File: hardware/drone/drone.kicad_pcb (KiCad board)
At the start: 2 copper layers, 2 parts, among them U1 STM32N645I0, U2 SX1262IMLTRT

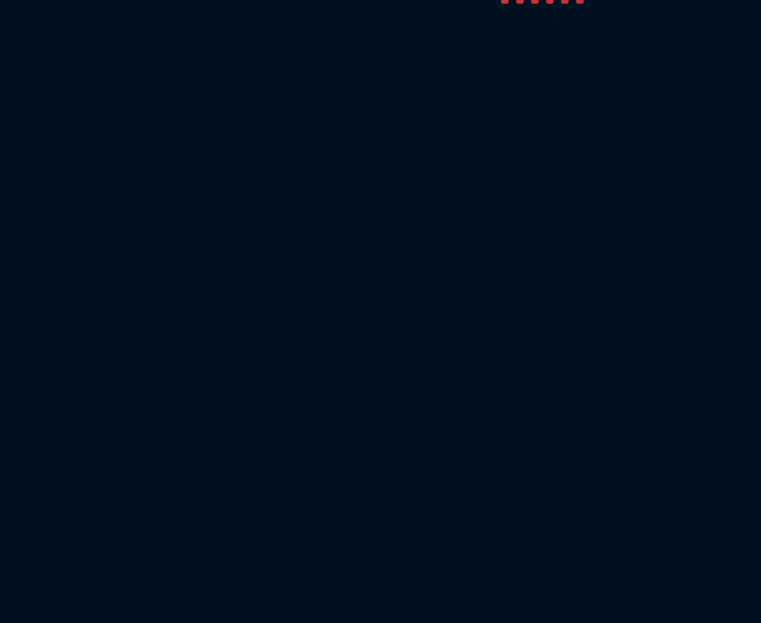
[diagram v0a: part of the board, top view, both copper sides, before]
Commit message: Continued PDN and started camera schematic
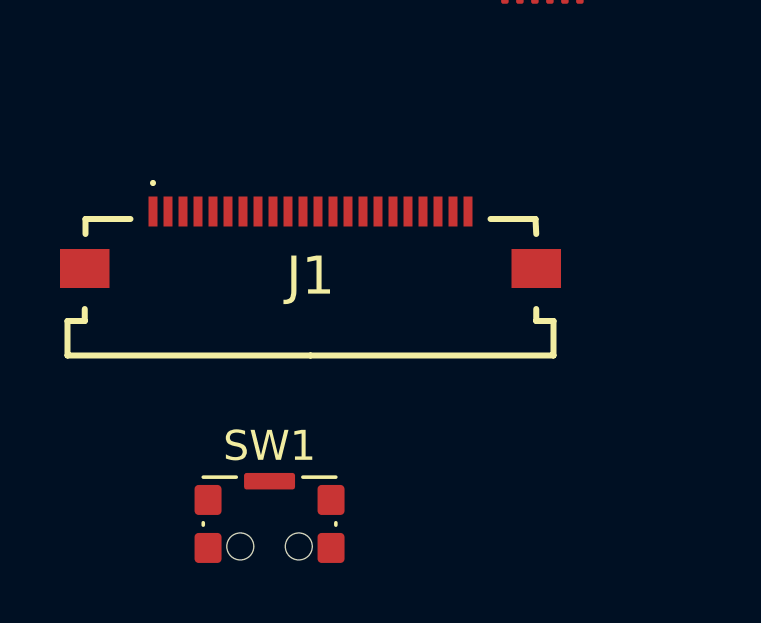
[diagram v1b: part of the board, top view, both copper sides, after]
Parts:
- added J1: 54548-2272, 54548-2272:545482272, F.Cu at (122.3, 106.8)
- added SW1: SW_MEC_5E, Button_Switch_SMD:SW_SPST_CK_KMS2xxGP, F.Cu at (120.9, 114.8)
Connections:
- U1 pad A1: (no net) -> unconnected-(U1MISC-PDR_ON-PadA1)
- U1 pad A14: unconnected-(U1Ground-VSS-PadA14) -> GND
- U1 pad A2: (no net) -> unconnected-(U1USB-OTG2_HSDM-PadA2)
- U1 pad A3: (no net) -> unconnected-(U1MISC-NC-PadA3)
- U1 pad A5: (no net) -> unconnected-(U1USB-OTG1_HSDM-PadA5)
- U1 pad A6: (no net) -> unconnected-(U1USB-UCPD1_CC1-PadA6)
- U1 pad B2: (no net) -> unconnected-(U1USB-OTG2_HSDP-PadB2)
- U1 pad B3: (no net) -> unconnected-(U1USB-OTG1_ID-PadB3)
- U1 pad B4: (no net) -> unconnected-(U1USB-OTG2_TXRTUNE-PadB4)
- U1 pad B5: (no net) -> unconnected-(U1USB-OTG1_HSDP-PadB5)
- U1 pad B6: (no net) -> unconnected-(U1USB-UCPD1_CC2-PadB6)
- U1 pad C4: (no net) -> unconnected-(U1MISC-NC-PadC4)
- U1 pad C5: (no net) -> unconnected-(U1USB-OTG2_ID-PadC5)
- U1 pad D2: unconnected-(U1Power-VFBSMPS-PadD2) -> VDDCORE
- U1 pad D3: (no net) -> unconnected-(U1MISC-BOOT0-PadD3)
- U1 pad D5: (no net) -> unconnected-(U1USB-OTG1_TXRTUNE-PadD5)
- U1 pad E3: (no net) -> unconnected-(U1MISC-PWR_ON-PadE3)
- U1 pad E4: (no net) -> /MCU/RESET
- U1 pad E7: unconnected-(U1Ground-VSS-PadE7) -> GND
- U1 pad F1: unconnected-(U1Ground-VSSSMPS-PadF1) -> GND
- U1 pad F10: unconnected-(U1Ground-VSS-PadF10) -> GND
- U1 pad F2: unconnected-(U1Ground-VSSSMPS-PadF2) -> GND
- U1 pad F3: unconnected-(U1Ground-VSSSMPS-PadF3) -> GND
- U1 pad F4: unconnected-(U1Ground-VSSSMPS-PadF4) -> GND
- U1 pad F5: unconnected-(U1Ground-VSSAON-PadF5) -> GND
- U1 pad G1: unconnected-(U1Power-VLXSMPS-PadG1) -> Net-(C6-Pad2)
- U1 pad G10: unconnected-(U1Power-VDD-PadG10) -> VDDIO
- U1 pad G11: unconnected-(U1Power-VDD-PadG11) -> VDDIO
- U1 pad G12: unconnected-(U1Power-VDD-PadG12) -> VDDIO
- U1 pad G2: unconnected-(U1Power-VLXSMPS-PadG2) -> Net-(C6-Pad2)
- U1 pad G3: unconnected-(U1Power-VLXSMPS-PadG3) -> Net-(C6-Pad2)
- U1 pad G4: unconnected-(U1Power-VLXSMPS-PadG4) -> Net-(C6-Pad2)
- U1 pad H1: unconnected-(U1Power-VDDSMPS-PadH1) -> VDD1V8_SMPS
- U1 pad H10: unconnected-(U1Ground-VSS-PadH10) -> GND
- U1 pad H11: unconnected-(U1Ground-VSS-PadH11) -> GND
- U1 pad H2: unconnected-(U1Power-VDDSMPS-PadH2) -> VDD1V8_SMPS
- U1 pad H3: unconnected-(U1Power-VDDSMPS-PadH3) -> VDD1V8_SMPS
- U1 pad H4: unconnected-(U1Power-VDDSMPS-PadH4) -> VDD1V8_SMPS
- U1 pad K10: unconnected-(U1Ground-VSS-PadK10) -> GND
- U1 pad K5: unconnected-(U1Ground-VSS-PadK5) -> GND
- U1 pad K6: unconnected-(U1Power-VDDCORE-PadK6) -> VDDCORE
- U1 pad K7: unconnected-(U1Power-VDDCORE-PadK7) -> VDDCORE
- U1 pad K8: unconnected-(U1Power-VDDCORE-PadK8) -> VDDCORE
- U1 pad K9: unconnected-(U1Power-VDDCORE-PadK9) -> VDDCORE
- U1 pad L7: unconnected-(U1Power-VDDCORE-PadL7) -> VDDCORE
- U1 pad M4: unconnected-(U1Ground-VSSA-PadM4) -> GND
- U1 pad N2: unconnected-(U1CSI-CSI_D1N-PadN2) -> /Camera/CSI_D1N
- U1 pad N3: unconnected-(U1CSI-CSI_CKN-PadN3) -> /Camera/CSI_CKN
- U1 pad N4: unconnected-(U1CSI-CSI_D0N-PadN4) -> /Camera/CSI_D0N
- U1 pad N6: unconnected-(U1Power-VDDCSI-PadN6) -> VDDCORE
- U1 pad P1: unconnected-(U1Ground-VSS-PadP1) -> GND
- U1 pad P14: unconnected-(U1Ground-VSS-PadP14) -> GND
- U1 pad P2: unconnected-(U1CSI-CSI_D1P-PadP2) -> /Camera/CSI_D1P
- U1 pad P3: unconnected-(U1CSI-CSI_CKP-PadP3) -> /Camera/CSI_CKP
- U1 pad P4: unconnected-(U1CSI-CSI_D0P-PadP4) -> /Camera/CSI_D0P

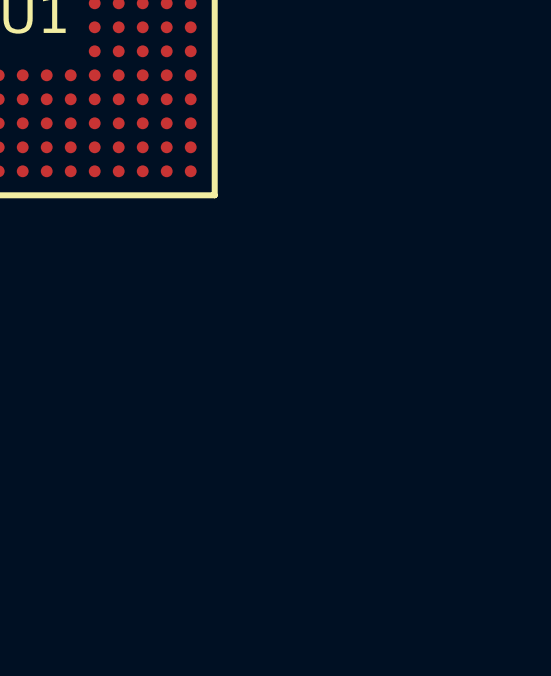
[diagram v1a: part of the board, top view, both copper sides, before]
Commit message: Created symbol for CC3350. Almost finished schematic for OSPI
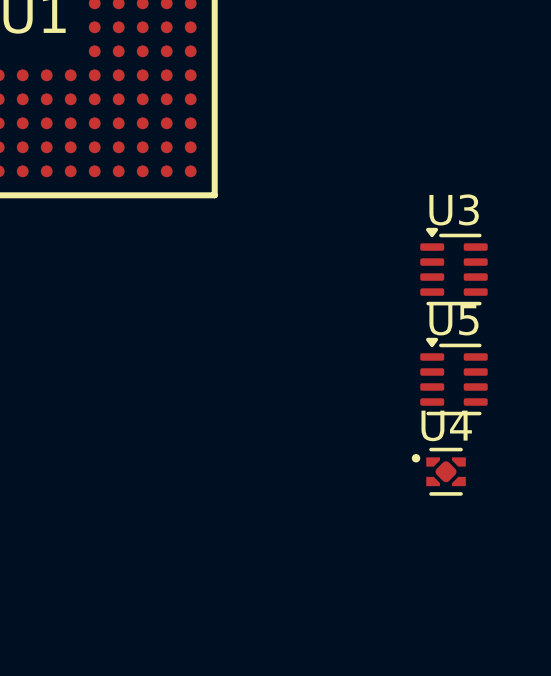
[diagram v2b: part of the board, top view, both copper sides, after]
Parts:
- added U3: TPS628303, Package_SON:Texas_VSON-HR-8_1.5x2mm_P0.5mm, F.Cu at (158.0, 104.0)
- added U4: TPS7A2118PQWDSGRQ1, Package_SON:Texas_X2SON-4_1x1mm_P0.65mm, F.Cu at (157.7, 110.7)
- added U5: TPS628303, Package_SON:Texas_VSON-HR-8_1.5x2mm_P0.5mm, F.Cu at (158.0, 107.7)
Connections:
- U1 pad A4: unconnected-(U1Power-VDD33USB-PadA4) -> GND
- U1 pad C2: unconnected-(U1Power-VBAT-PadC2) -> VDDA1V8
- U1 pad D1: unconnected-(U1Power-V08CAP-PadD1) -> Net-(U1Power-V08CAP)
- U1 pad D4: unconnected-(U1Power-VDDA18USB-PadD4) -> GND
- U1 pad E1: unconnected-(U1Power-VDDA18PMU-PadE1) -> VDDA1V8PMU
- U1 pad E5: unconnected-(U1Power-VDDA18AON-PadE5) -> VDDA1V8
- U1 pad E8: unconnected-(U1Power-VDDIO4-PadE8) -> VDD1V8
- U1 pad E9: unconnected-(U1Power-VDDIO4-PadE9) -> VDD1V8
- U1 pad G10: VDDIO -> VDDA1V8
- U1 pad G11: VDDIO -> VDDA1V8
- U1 pad G12: VDDIO -> VDDA1V8
- U1 pad H1: VDD1V8_SMPS -> VDD1V8
- U1 pad H2: VDD1V8_SMPS -> VDD1V8
- U1 pad H3: VDD1V8_SMPS -> VDD1V8
- U1 pad H4: VDD1V8_SMPS -> VDD1V8
- U1 pad J10: unconnected-(U1Power-VDDIO3-PadJ10) -> VDD1V8
- U1 pad J11: unconnected-(U1Power-VDDIO3-PadJ11) -> VDD1V8
- U1 pad M1: unconnected-(U1Power-VREF+-PadM1) -> VDD1V8
- U1 pad M3: unconnected-(U1Power-VDDA18ADC-PadM3) -> VDD1V8
- U1 pad N1: unconnected-(U1Power-VREF--PadN1) -> GND
- U1 pad P5: unconnected-(U1Power-VDDA18CSI-PadP5) -> VDD1V8

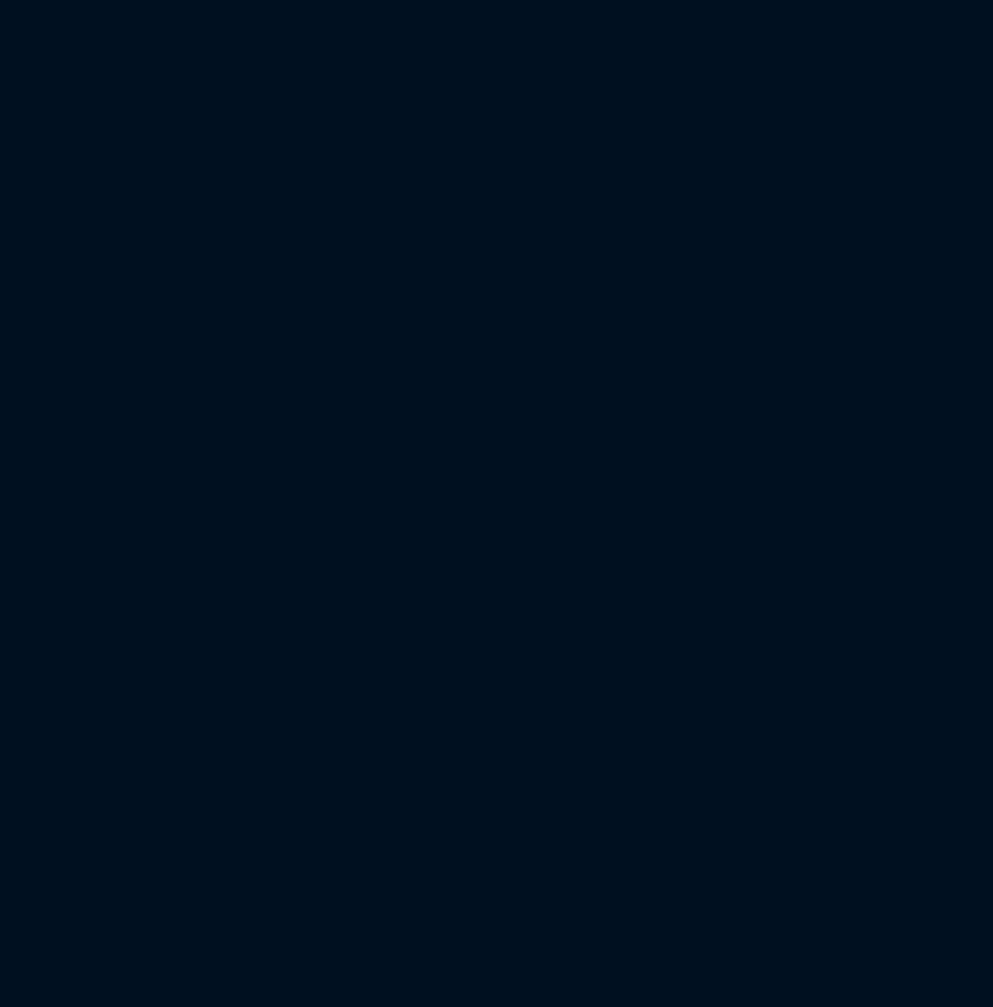
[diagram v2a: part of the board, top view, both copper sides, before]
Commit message: Fixed SMPS and LDO sequencing issues
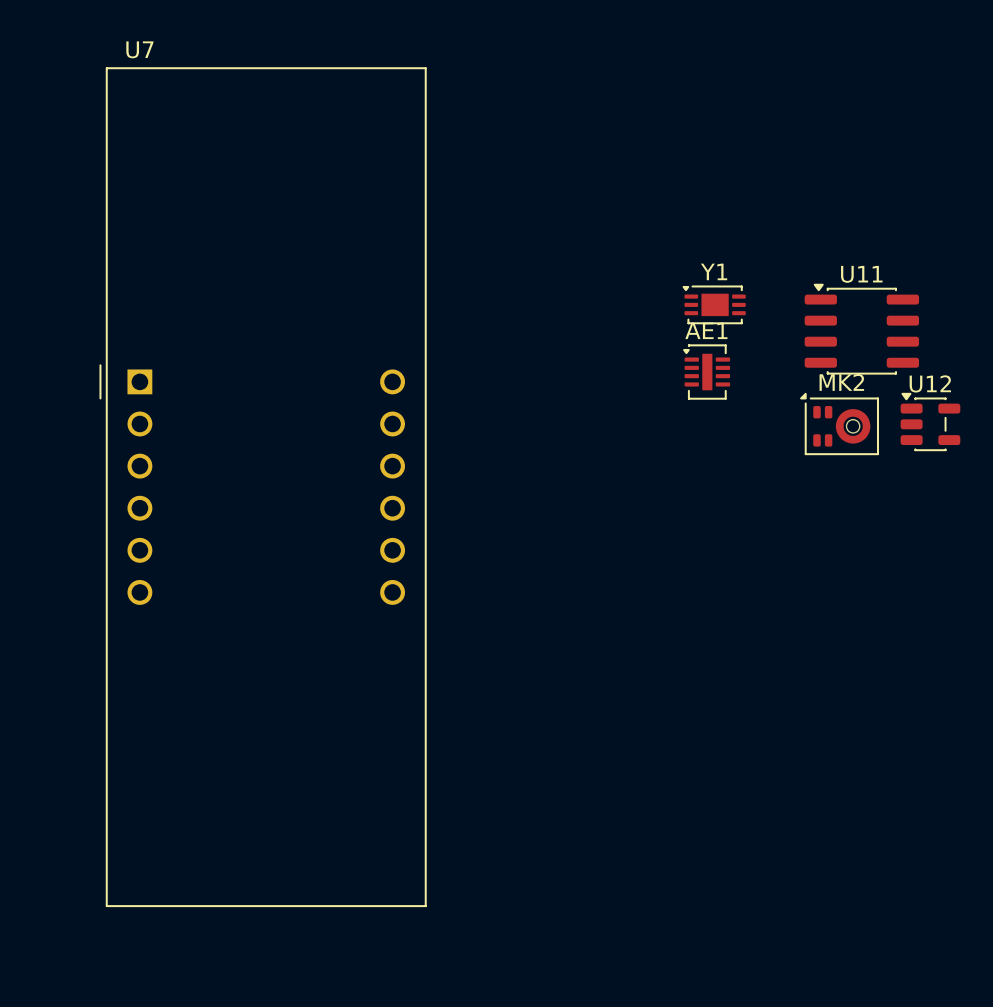
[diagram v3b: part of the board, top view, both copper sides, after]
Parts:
- added AE1: Antenna, Package_DFN_QFN:DFN-8-1EP_2x3mm_P0.5mm_EP0.61x2.2mm, F.Cu at (186.5, 49.8)
- added MK2: IM73A135V01, Sensor_Audio:Infineon_PG-LLGA-5-2, F.Cu at (194.6, 53.1)
- added U11: TAC5111, Package_SO:SOIC-8_3.9x4.9mm_P1.27mm, F.Cu at (195.8, 47.4)
- added U12: LM4670SD/NOPB, Package_TO_SOT_SMD:SOT-23-5, F.Cu at (199.9, 53.0)
- added U7: CC3350, Display_7Segment:CC56-12GWA, F.Cu at (152.3, 50.4)
- added Y1: Crystal_GND24, Package_DFN_QFN:DFN-6-1EP_3x2mm_P0.5mm_EP1.65x1.35mm, F.Cu at (187.0, 45.8)
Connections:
- U2 pad 1: unconnected-(U2-VDD_IN-Pad1) -> VDD3V3
- U2 pad 10: unconnected-(U2-VBAT-Pad10) -> VDD3V3
- U2 pad 11: unconnected-(U2-VBAT_IO-Pad11) -> VDD1V8
- U2 pad 12: unconnected-(U2-DIO2-Pad12) -> /RF_915/SX_DIO2
- U2 pad 13: unconnected-(U2-DIO1-Pad13) -> SX_IRQ
- U2 pad 14: unconnected-(U2-BUSY-Pad14) -> SX_BUSY
- U2 pad 16: unconnected-(U2-MISO-Pad16) -> SX_SPI5_MISO
- U2 pad 17: unconnected-(U2-MOSI-Pad17) -> SX_SPI5_MOSI
- U2 pad 18: unconnected-(U2-SCK-Pad18) -> SX_SPI5_SCK
- U2 pad 19: unconnected-(U2-NSS-Pad19) -> SX_SPI5_NSS
- U2 pad 2: Net-(U2-GND-Pad2) -> GND
- U2 pad 20: Net-(U2-GND-Pad2) -> GND
- U2 pad 21: unconnected-(U2-RFI_P-Pad21) -> Net-(U2-RFI_P)
- U2 pad 22: unconnected-(U2-RFI_N-Pad22) -> Net-(U2-RFI_N)
- U2 pad 23: unconnected-(U2-RFO-Pad23) -> Net-(U2-RFO)
- U2 pad 24: unconnected-(U2-VR_PA-Pad24) -> Net-(U2-VR_PA)
- U2 pad 25: Net-(U2-GND-Pad2) -> GND
- U2 pad 3: unconnected-(U2-XTA-Pad3) -> Net-(U2-XTA)
- U2 pad 4: unconnected-(U2-XTB-Pad4) -> Net-(U2-XTB)
- U2 pad 5: Net-(U2-GND-Pad2) -> GND
- U2 pad 7: unconnected-(U2-VREG-Pad7) -> Net-(U2-VREG)
- U2 pad 8: Net-(U2-GND-Pad2) -> GND
- U2 pad 9: unconnected-(U2-DCC_SW-Pad9) -> Net-(U2-DCC_SW)

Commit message: Added SWD
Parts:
- removed AE1: Antenna, Package_DFN_QFN:DFN-8-1EP_2x3mm_P0.5mm_EP0.61x2.2mm
- removed J1: 54548-2272, 54548-2272:545482272
- removed MK2: IM73A135V01, Sensor_Audio:Infineon_PG-LLGA-5-2
- removed SW1: SW_MEC_5E, Button_Switch_SMD:SW_SPST_CK_KMS2xxGP
- removed U1: STM32N645I0, STM32N645I0:BGA178C80P14X14_1200X1200X100
- removed U11: TAC5111, Package_SO:SOIC-8_3.9x4.9mm_P1.27mm
- removed U12: LM4670SD/NOPB, Package_TO_SOT_SMD:SOT-23-5
- removed U2: SX1262IMLTRT, Package_DFN_QFN:QFN-24-1EP_4x4mm_P0.5mm_EP2.6x2.6mm
- removed U3, U5: TPS628303, Package_SON:Texas_VSON-HR-8_1.5x2mm_P0.5mm
- removed U4: TPS7A2118PQWDSGRQ1, Package_SON:Texas_X2SON-4_1x1mm_P0.65mm
- removed U7: CC3350, Display_7Segment:CC56-12GWA
- removed Y1: Crystal_GND24, Package_DFN_QFN:DFN-6-1EP_3x2mm_P0.5mm_EP1.65x1.35mm

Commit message: Small cleanup
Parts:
- added C118: 220n, Package_LGA:LGA-12_2x2mm_P0.5mm, F.Cu at (171.2, 85.4)
- added C97: 10u, Connector:Tag-Connect_TC2030-IDC-FP_2x03_P1.27mm_Vertical, F.Cu at (116.6, 65.8)
- added C98: 100n, Connector:Tag-Connect_TC2030-IDC-FP_2x03_P1.27mm_Vertical, F.Cu at (125.6, 65.8)
- added J1: 54548-2272, 54548-2272:545482272, F.Cu at (127.3, 128.0)
- added J4: Conn_ARM_SWD_TagConnect_TC2030, Connector:Tag-Connect_TC2030-IDC-FP_2x03_P1.27mm_Vertical, F.Cu at (173.4, 33.8)
- added J5: Conn_01x06_Pin, RF_Module:Ai-Thinker-Ra-01-LoRa, F.Cu at (105.6, 92.9)
- added MK2: IM73A135V01, Sensor_Audio:Infineon_PG-LLGA-5-2, F.Cu at (154.3, 92.5)
- added Q1: ISP650P06NM, Package_DIP:DIP-24_W7.62mm, F.Cu at (113.4, 31.0)
- added SW1: SW_MEC_5E, Button_Switch_SMD:SW_SPST_CK_KMS2xxGP, F.Cu at (171.9, 41.0)
- added U1: STM32N645I0, STM32N645I0:BGA178C80P14X14_1200X1200X100, F.Cu at (249.3, 54.0)
- added U11: TAC5111, Package_SO:SOIC-8_3.9x4.9mm_P1.27mm, F.Cu at (155.6, 86.7)
- added U12: LM4670SD/NOPB, Package_TO_SOT_SMD:SOT-23-5, F.Cu at (159.7, 92.3)
- added U14: ICM-42688-P, Package_LGA:LGA-16_3x3mm_P0.5mm_LayoutBorder3x5y, F.Cu at (166.9, 85.6)
- added U15: SAM_M10Q, Package_LGA:LGA-16_3x3mm_P0.5mm_LayoutBorder3x5y, F.Cu at (166.9, 90.2)
- added U16: LMR51635XFDDCR, Package_TO_SOT_SMD:SOT-23-6, F.Cu at (118.2, 73.0)
- added U18: TPS2121, Package_TO_SOT_SMD:SOT-583-8, F.Cu at (117.4, 77.2)
- added U2: SX1262IMLTRT, Package_DFN_QFN:QFN-24-1EP_4x4mm_P0.5mm_EP2.6x2.6mm, F.Cu at (120.9, 118.4)
- added U20: TVS0500DRV, Package_SON:WSON-6-1EP_2x2mm_P0.65mm_EP1x1.6mm, F.Cu at (170.5, 45.8)
- added U22: LIS2MDL, Package_LGA:LGA-12_2x2mm_P0.5mm, F.Cu at (171.2, 89.2)
- added U3: TPS628303, Package_SON:Texas_VSON-HR-8_1.5x2mm_P0.5mm, F.Cu at (113.7, 72.5)
- added U4: TPS7A2118PQWDSGRQ1, Package_SON:Texas_X2SON-4_1x1mm_P0.65mm, F.Cu at (122.4, 71.9)
- added U5: TPS628303, Package_SON:Texas_VSON-HR-8_1.5x2mm_P0.5mm, F.Cu at (113.7, 76.1)
- added Y1: Crystal_GND24, Package_DFN_QFN:DFN-6-1EP_3x2mm_P0.5mm_EP1.65x1.35mm, F.Cu at (98.5, 104.2)

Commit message: Started footprint assignments
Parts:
- removed C118: 220n, Package_LGA:LGA-12_2x2mm_P0.5mm
- removed C97: 10u, Connector:Tag-Connect_TC2030-IDC-FP_2x03_P1.27mm_Vertical
- removed C98: 100n, Connector:Tag-Connect_TC2030-IDC-FP_2x03_P1.27mm_Vertical
- removed J5: Conn_01x06_Pin, RF_Module:Ai-Thinker-Ra-01-LoRa
- removed SW1: SW_MEC_5E, Button_Switch_SMD:SW_SPST_CK_KMS2xxGP
- removed U12: LM4670SD/NOPB, Package_TO_SOT_SMD:SOT-23-5
- removed U14: ICM-42688-P, Package_LGA:LGA-16_3x3mm_P0.5mm_LayoutBorder3x5y
- removed U15: SAM_M10Q, Package_LGA:LGA-16_3x3mm_P0.5mm_LayoutBorder3x5y
- removed U16: LMR51635XFDDCR, Package_TO_SOT_SMD:SOT-23-6
- removed U18: TPS2121, Package_TO_SOT_SMD:SOT-583-8
- removed Y1: Crystal_GND24, Package_DFN_QFN:DFN-6-1EP_3x2mm_P0.5mm_EP1.65x1.35mm
- added J2: BM08B-SRSS-TB_LF__SN_, BM08B-SRSS-TB_LF__SN_:BM08BSRSSTBLFSN, F.Cu at (76.5, 63.3)
- added TP1: TestPoint, TestPoint:TestPoint_Pad_2.0x2.0mm, F.Cu at (39.5, 111.5)
- added TP2: TestPoint, TestPoint:TestPoint_Pad_2.0x2.0mm, F.Cu at (39.5, 115.6)
- added TP3: TestPoint, TestPoint:TestPoint_Pad_2.0x2.0mm, F.Cu at (39.5, 119.6)
- added TP4: TestPoint, TestPoint:TestPoint_Pad_2.0x2.0mm, F.Cu at (39.5, 123.7)
- added TP5: TestPoint, TestPoint:TestPoint_Pad_2.0x2.0mm, F.Cu at (43.6, 111.5)
- added TP6: TestPoint, TestPoint:TestPoint_Pad_2.0x2.0mm, F.Cu at (43.6, 115.6)
- added TP7: TestPoint, TestPoint:TestPoint_Pad_2.0x2.0mm, F.Cu at (43.6, 119.6)
- added U10: PE4259, PE4259-63:SOT65P210X110-6N, F.Cu at (42.4, 103.0)
- added U6: MX25UW25645GXDI00, MX25UW25645GXDI00:BGA24C100P5X5_600X800X120, F.Cu at (62.8, 91.1)
- added U7: CC3350, CC3350ENJARSBR:QFN40P500X500X80-41N-D, F.Cu at (81.4, 101.3)
- added U8: DPX167125DT-8197B1, DPX167125DT-8197B1:DPX167125DT8197B1, F.Cu at (61.5, 103.3)
- added U9: DEA162450BT-1295A1, DEA162450BT-1295A1:DEA162450BT1295A1, F.Cu at (77.5, 91.5)
- Q1: footprint Package_DIP:DIP-24_W7.62mm -> Package_TO_SOT_SMD:SOT-223
- U11: value TAC5111 -> TAC5111IRGER; footprint Package_SO:SOIC-8_3.9x4.9mm_P1.27mm -> SoftDroneLibrary:TAC5111IRGER
- U2: footprint Package_DFN_QFN:QFN-24-1EP_4x4mm_P0.5mm_EP2.6x2.6mm -> Package_DFN_QFN:QFN-24-1EP_4x4mm_P0.5mm_EP2.7x2.7mm
- U3, U5: footprint Package_SON:Texas_VSON-HR-8_1.5x2mm_P0.5mm -> TPS628303ARZER:WQFN-HR8_RZE_TEX
- U4: footprint Package_SON:Texas_X2SON-4_1x1mm_P0.65mm -> Package_SON:Texas_DSG0008A_WSON-8-1EP_2x2mm_P0.5mm_EP0.9x1.6mm
- moved U1 189.7 mm to (60.0, 66.9)
- moved J4 108.2 mm to (74.3, 77.3)
- moved U22 101.7 mm to (71.6, 68.7)
- moved MK2 99.7 mm to (55.5, 79.0)
- moved J1 98.8 mm to (62.4, 53.5)
- moved U20 94.5 mm to (80.5, 74.4)
- moved Q1 93.8 mm to (41.4, 91.2)
- moved U5 79.8 mm to (52.9, 127.8)
- moved U3 76.5 mm to (56.6, 123.3)
- moved U11 72.9 mm to (86.8, 111.1)
- moved U2 68.8 mm to (52.2, 115.2)
- moved U4 67.8 mm to (68.1, 112.5)
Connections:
- J1 pad 2: /Camera/CSI_D0N -> /Camera/CSI_D0N_CON
- J1 pad 3: /Camera/CSI_D0P -> /Camera/CSI_D0P_CON
- J1 pad 5: /Camera/CSI_D1N -> /Camera/CSI_D1N_CON
- J1 pad 6: /Camera/CSI_D1P -> /Camera/CSI_D1P_CON
- J1 pad 8: /Camera/CSI_CKN -> /Camera/CSI_CKN_CON
- J1 pad 9: /Camera/CSI_CKP -> /Camera/CSI_CKP_CON
- U1 pad A4: GND -> VDD3V3
- U1 pad B1: unconnected-(U1PC-PC14-OSC32_IN-PadB1) -> Net-(U1PC-PC14-OSC32_IN)
- U1 pad C1: unconnected-(U1PC-PC15-OSC32_OUT-PadC1) -> Net-(U1PC-PC15-OSC32_OUT)
- U1 pad D4: GND -> VDDA1V8
- U1 pad E12: unconnected-(U1PB-PB3-PadE12) -> IMU_INT2
- U1 pad E13: unconnected-(U1PB-PB2-PadE13) -> IMU_INT1
- U1 pad J12: unconnected-(U1PN-PN12-PadJ12) -> /MCU/OSPI_NRESET
- U1 pad M10: IMU_INT1 -> unconnected-(U1PB-PB12-PadM10)
